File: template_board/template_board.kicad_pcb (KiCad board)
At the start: 4 copper layers, 100 x 100 mm, 112 parts, among them J1 USB_C_Receptacle_USB2.0_16P, J2 PTHF-130-02-G-Q-368, J4 SWD, Q2 MMST3904, Q3 AO3400A, SW1 SW_Push, SW2 SW_DIP_x01, SW3 SW_Push, U1 IP4220CZ6, U11 FSUSB42UMX, U12 CH334P, U2 LM74700, U3 IP4220CZ6, U4 AZ1117-3.3, U5 STM32U575RITx, U6 TJA1145T, U7 STM32F103CBTx, X3 Q13FC1350000400, X4 X322512MSB4SI, Y5 8 MHz, Y6 12Mhz

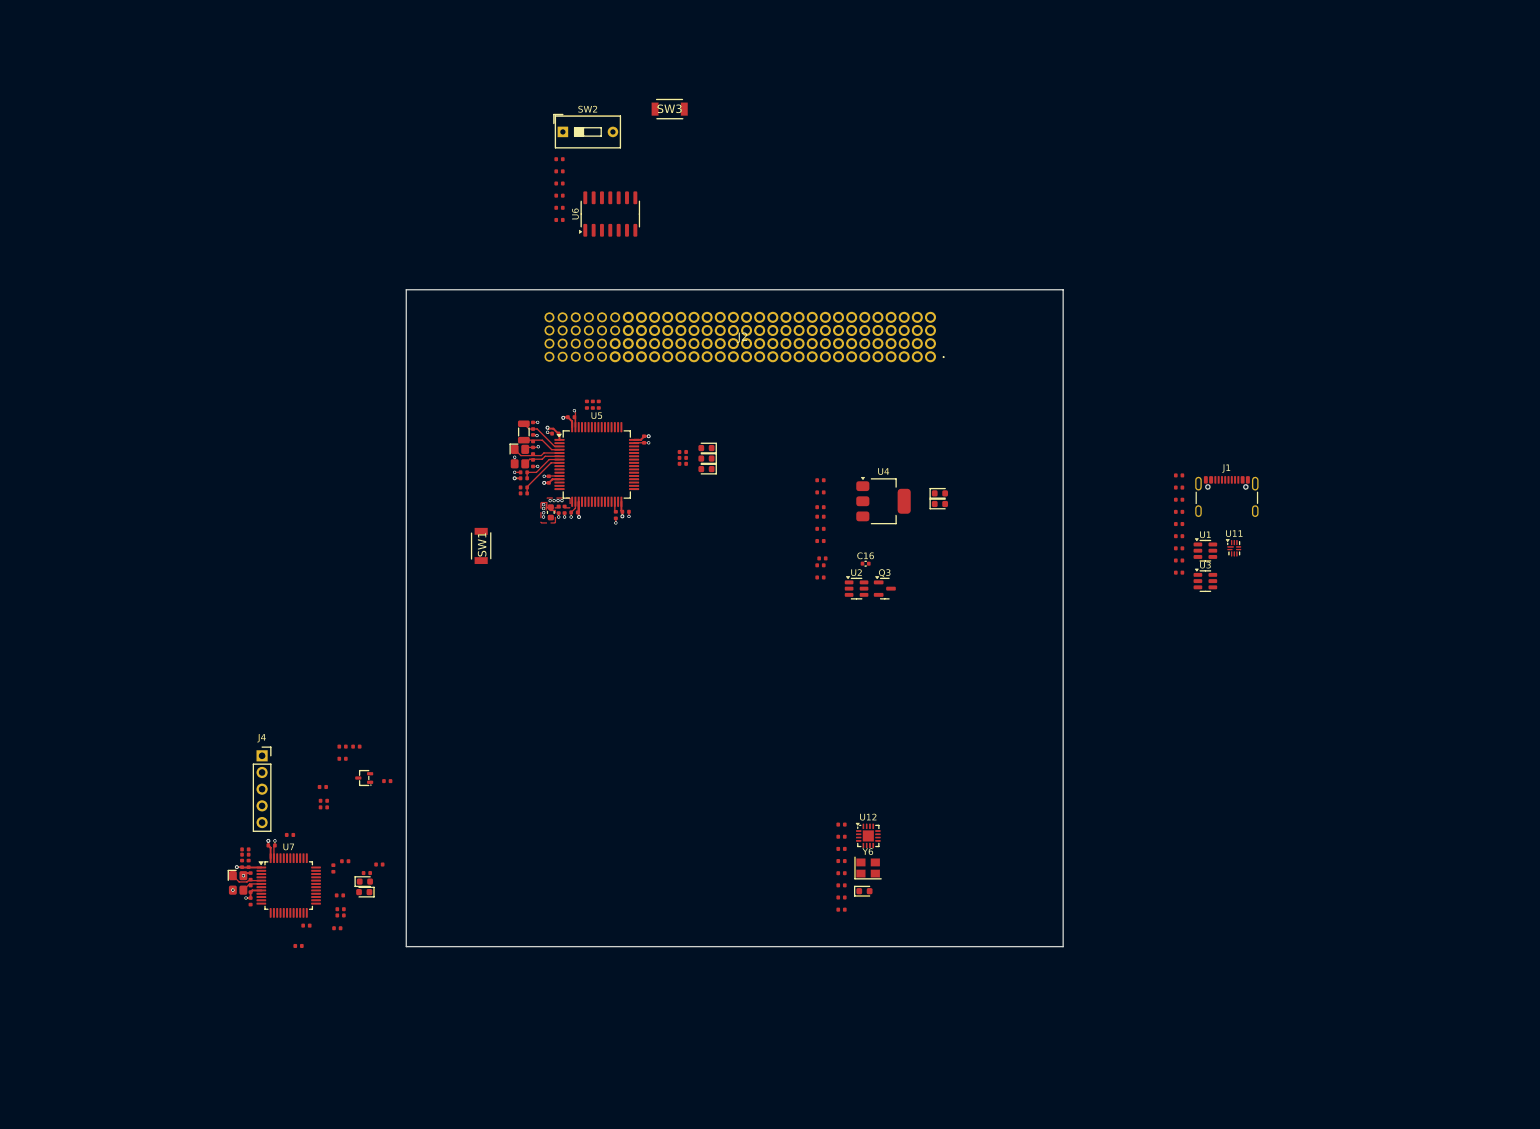
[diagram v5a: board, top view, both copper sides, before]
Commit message: sub leyoyut partially completed
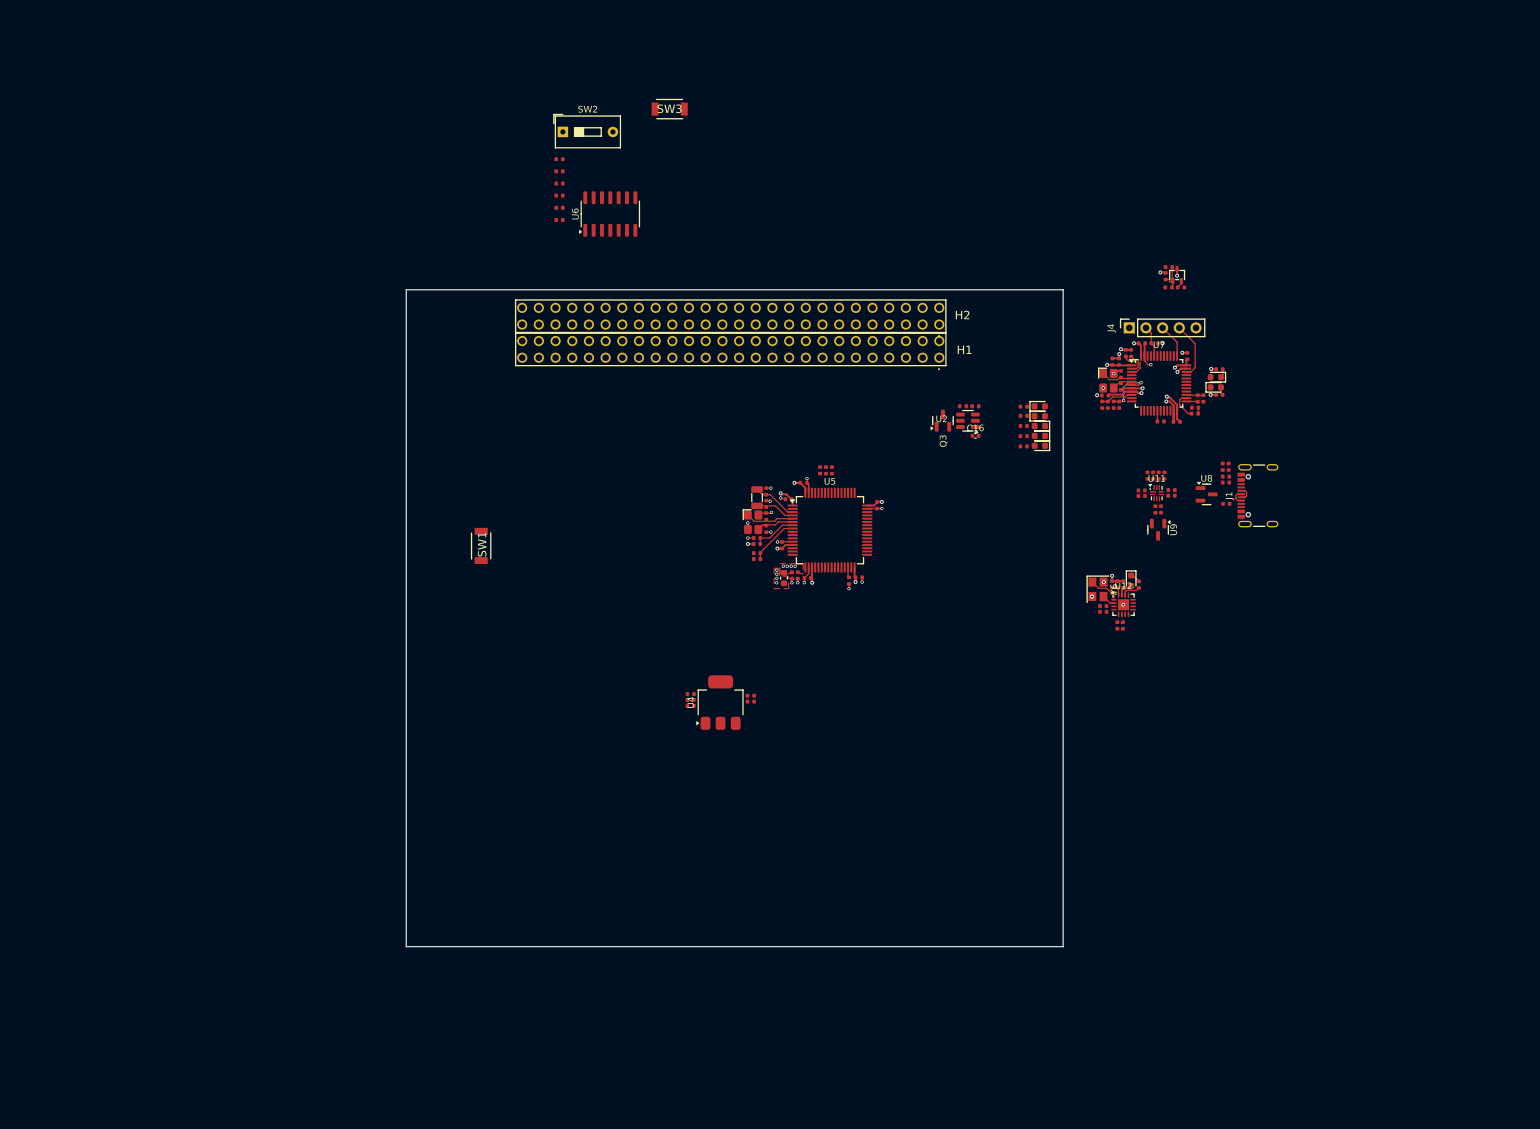
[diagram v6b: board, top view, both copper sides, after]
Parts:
- removed J2: PTHF-130-02-G-Q-368, lib:PTHF13002GQ368
- removed U1, U3: IP4220CZ6, Package_TO_SOT_SMD:SOT-23-6
- added H1: ESQ-126-14-G-D, lib:ESQ-126-Y-X-D, F.Cu at (159.2, 70.3)
- added H2: ESQ-126-14-G-D, lib:ESQ-126-Y-X-D, F.Cu at (159.1, 65.3)
- added R15: 22Ω, PCM_JLCPCB:R_0402, F.Cu at (194.5, 90.5)
- added R16: 22Ω, PCM_JLCPCB:R_0402, F.Cu at (194.5, 91.3)
- added R17: 22Ω, PCM_JLCPCB:R_0402, F.Cu at (192.9, 93.4)
- added R18: 22Ω, PCM_JLCPCB:R_0402, F.Cu at (192.1, 93.4)
- added R19: 22Ω, PCM_JLCPCB:R_0402, F.Cu at (189.9, 90.5)
- added R20: 22Ω, PCM_JLCPCB:R_0402, F.Cu at (189.9, 91.4)
- added U8: PESD5V0S2BT, Package_TO_SOT_SMD:SOT-23, F.Cu at (199.8, 91.2)
- added U9: PESD5V0S2BT, Package_TO_SOT_SMD:SOT-23, F.Cu at (192.4, 96.5)
- moved R44 159.2 mm to (198.1, 78.0)
- moved R28 154.6 mm to (188.3, 69.7), turned to -90 degrees
- moved R26 154.3 mm to (187.5, 69.7), turned to -90 degrees
- moved R54 153.4 mm to (193.6, 58.0), turned to 90 degrees
- moved R9 153.1 mm to (199.3, 76.6), turned to 90 degrees
- moved C26 153.1 mm to (195.3, 80.1)
- moved C43 153.0 mm to (186.5, 71.0)
- moved C6 153.0 mm to (186.8, 72.9)
- moved C7 153.0 mm to (185.5, 71.0)
- moved Y5 153.0 mm to (184.9, 73.9)
- moved C35 153.0 mm to (190.0, 68.2)
- moved C8 153.0 mm to (186.8, 74.8)
- moved U7 153.0 mm to (192.6, 74.3)
- moved C34 151.6 mm to (196.9, 70.1), turned to 90 degrees
- moved D8 151.5 mm to (201.2, 73.3)
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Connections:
- J4 pad 1: unconnected-(J4-Pin_1-Pad1) -> +3V3
- J4 pad 2: unconnected-(J4-Pin_2-Pad2) -> /ST-LINK/STLINK-BOOT0
- J4 pad 3: unconnected-(J4-Pin_3-Pad3) -> /ST-LINK/CLK
- J4 pad 4: unconnected-(J4-Pin_4-Pad4) -> /ST-LINK/DIO
- J4 pad 5: unconnected-(J4-Pin_5-Pad5) -> GND
- U11 pad 1: /USB-C/EXTUSB.D+ -> Net-(U11-D+)
- U11 pad 2: /USB-C/EXTUSB.D- -> Net-(U11-D-)
- U11 pad 4: /USB-C/BACKPLANE.D- -> Net-(U11-HSD1-)
- U11 pad 5: /USB-C/BACKPLANE.D+ -> Net-(U11-HSD1+)
- U11 pad 6: /USB-C/USB2S.D- -> Net-(U11-HSD2-)
- U11 pad 7: /USB-C/USB2S.D+ -> Net-(U11-HSD2+)
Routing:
- net GND: track 28.0 -> 47.1 mm, vias 19 -> 31
- net +3V3: track 7.44 -> 22.4 mm, vias 7 -> 12
- net /ST-LINK/DIO: track 0.00 -> 8.66 mm
- net /ST-LINK/STLINK-RST: track 0.00 -> 8.06 mm, vias 0 -> 2
- net /ST-LINK/CLK: track 0.00 -> 5.20 mm
- net Net-(U7-PA0): track 0.00 -> 4.90 mm, vias 0 -> 1
- net /ST-LINK/STLINK-BOOT0: track 0.00 -> 4.80 mm
- net Net-(U12-XO): track 0.00 -> 4.76 mm
- net Net-(Q2-B): track 0.00 -> 4.39 mm
- net Net-(U7-PB13): track 0.00 -> 4.24 mm
- net Net-(U7-PC14): track 0.00 -> 4.07 mm
- net Net-(U7-PC13): track 0.00 -> 4.04 mm
- net Net-(U12-PGANG): track 0.00 -> 2.87 mm
- net Net-(U7-PB14): track 0.00 -> 2.61 mm
- net +5V: track 0.00 -> 2.53 mm
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
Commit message: layout 95% completed
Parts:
- added M1: MountingHole, MountingHole:MountingHole_3.2mm_M3_Pad, F.Cu at (27.1, 23.0)
- added M2: MountingHole, MountingHole:MountingHole_3.2mm_M3_Pad, F.Cu at (100.7, 23.0)
- added M3: MountingHole, MountingHole:MountingHole_3.2mm_M3_Pad, F.Cu at (103.2, 108.8)
- added M4: MountingHole, MountingHole:MountingHole_3.2mm_M3_Pad, F.Cu at (23.2, 108.8)
- moved R52 107.4 mm to (90.7, 38.5)
- moved R55 107.4 mm to (88.8, 38.5)
- moved Q2 107.0 mm to (90.4, 36.6)
- moved R53 107.0 mm to (89.2, 35.4)
- moved R54 107.0 mm to (88.7, 36.8)
- moved R8 106.7 mm to (94.5, 53.0)
- moved C7 106.5 mm to (81.9, 46.3)
- moved C25 106.4 mm to (80.9, 51.2)
- moved C34 106.4 mm to (93.4, 45.2)
- moved C35 106.4 mm to (86.5, 43.2)
- moved C43 106.4 mm to (83.0, 46.0)
- moved R10 106.4 mm to (88.4, 43.2)
- moved R25 106.4 mm to (95.0, 51.6)
- moved R28 106.4 mm to (84.8, 44.8)
- moved R37 106.4 mm to (89.3, 55.1)
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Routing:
- net +5V: track 2.53 -> 87.4 mm, vias 0 -> 2
- net GND: track 47.1 -> 102.1 mm, vias 31 -> 69
- net +5V_unprotected: track 0.00 -> 52.4 mm, vias 0 -> 2
- net /MCU/SWD.~{RST}: track 6.83 -> 59.0 mm, vias 0 -> 3
- net /can_tranciver/WAKE: track 0.00 -> 46.3 mm, vias 0 -> 2
- net /BUS_CONNECTOR/CAN1.-: track 0.00 -> 36.0 mm, vias 0 -> 1
- net /MCU/USER_LED_1: track 0.00 -> 35.4 mm
- net /BUS_CONNECTOR/CAN1.+: track 0.00 -> 34.4 mm, vias 0 -> 1
- net /MCU/USB_MCU.D-: track 0.00 -> 33.3 mm, vias 0 -> 2
- net /MCU/USB_MCU.D+: track 0.00 -> 32.5 mm, vias 0 -> 2
- net /MCU/USER_LED_2: track 0.00 -> 32.4 mm
- net /MCU/STATUS_LED: track 0.00 -> 31.3 mm
- net /USB-C/USB2S.D-: track 2.32 -> 30.3 mm
- net /USB-C/USB2S.D+: track 2.35 -> 28.6 mm
- net +3V3: track 22.4 -> 46.8 mm, vias 12 -> 19
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- added copper zone on In1.Cu, net (none)
- added copper zone on In2.Cu, net (none)
- added copper zone on In2.Cu, net +3V3
- added copper zone on In1.Cu, net GND
- removed copper zone on In2.Cu, net /MCU/+VDDA
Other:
- board size 100 x 100 mm -> 90.2 x 95.9 mm

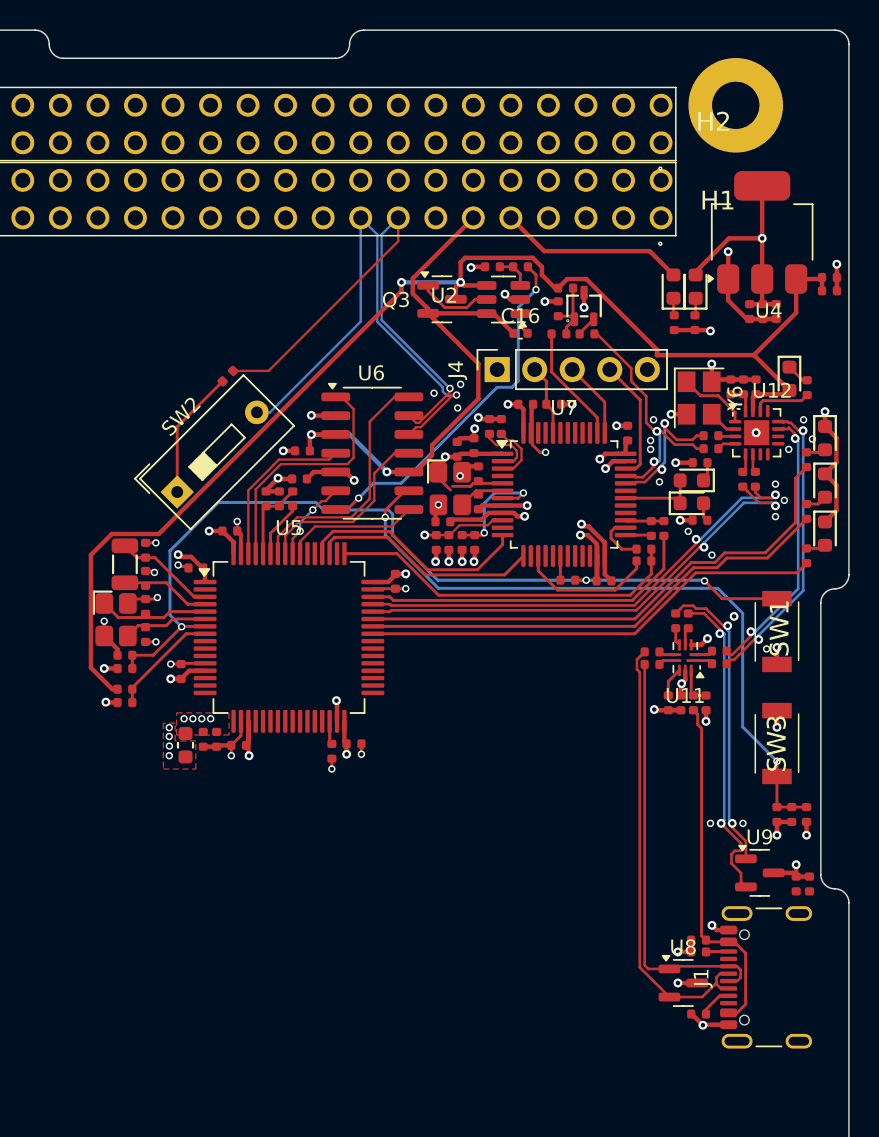
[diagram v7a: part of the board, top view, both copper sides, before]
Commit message: drc fixed
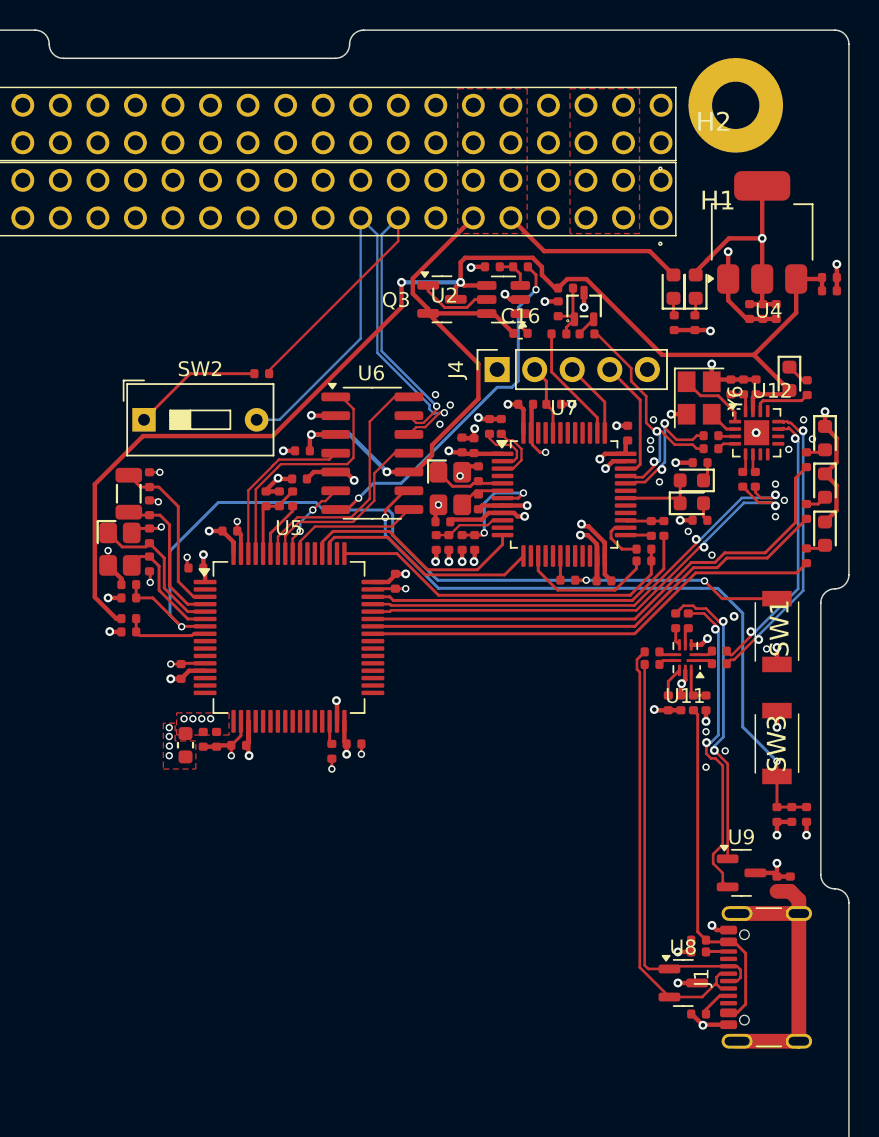
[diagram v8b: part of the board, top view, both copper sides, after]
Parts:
- moved SW2 5.38 mm to (60.7, 44.3), turned to 0 degrees
- moved C2 4.78 mm to (59.6, 55.4)
- moved C60 4.78 mm to (61.0, 54.0)
- moved R5 4.78 mm to (59.6, 56.3)
- moved X4 4.78 mm to (59.0, 53.0)
- moved C51 4.78 mm to (61.0, 50.2)
- moved C58 4.78 mm to (61.0, 52.1)
- moved C59 4.78 mm to (61.0, 48.3)
- moved R27 4.78 mm to (59.6, 57.7)
- moved R6 4.78 mm to (59.6, 58.6)
- moved X3 4.78 mm to (59.6, 49.3)
- moved R2 2.30 mm to (68.6, 41.2), turned to 180 degrees
- moved C44 1.30 mm to (103.5, 75.7)
- moved R56 1.30 mm to (104.4, 75.7)
- moved U9 1.24 mm to (101.1, 75.0)
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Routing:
- net Net-(J1-SHIELD): track 0.00 -> 19.6 mm
- net /MCU/OSC32_IN: track 6.85 -> 11.5 mm
- net /MCU/OSC32_OUT: track 6.03 -> 10.2 mm
- net /BUS_CONNECTOR/CAN1.+: track 34.4 -> 31.6 mm
- net /MCU/OSC_IN: track 7.38 -> 10.2 mm
- net /MCU/OSC_OUT: track 5.70 -> 7.91 mm
- net +5V: track 87.4 -> 85.5 mm
- net /MCU/V_SENSE: track 7.44 -> 5.82 mm
- net /MCU/+VDDA: track 17.1 -> 16.0 mm
- net Net-(U7-PA0): track 5.68 -> 4.90 mm, vias 1 -> 0
- net /USB-C/BACKPLANE.D-: track 22.3 -> 21.8 mm
- net GND: track 102.1 -> 102.2 mm, vias 69 -> 70
- added copper zone on F.Cu, net +5V_unprotected
- added copper zone on F.Cu, net +VBAT
- added copper zone on In2.Cu, net /MCU/+VDDA
